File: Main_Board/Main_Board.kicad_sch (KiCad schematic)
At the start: 0 parts

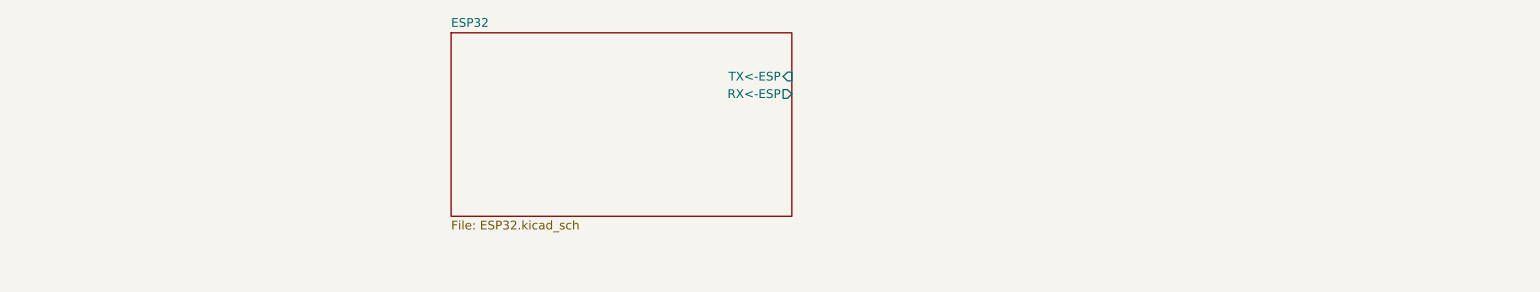
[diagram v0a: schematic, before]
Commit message: PSU Ready + ESP32 advanced
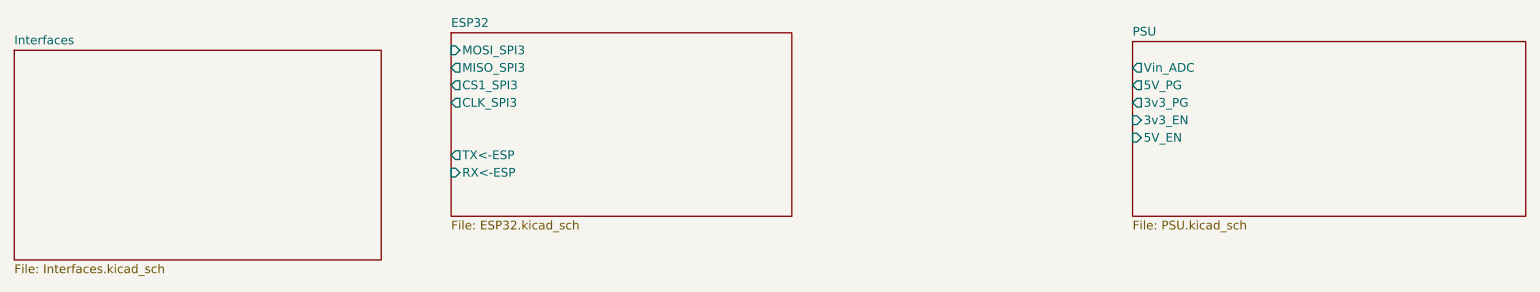
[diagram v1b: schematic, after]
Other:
- added sheet Interfaces (Interfaces.kicad_sch)
- added sheet PSU (PSU.kicad_sch)
- sheet ESP32 ports: added CLK_SPI3, CS1_SPI3, MISO_SPI3, MOSI_SPI3; removed none
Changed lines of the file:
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@@
 	(paper "A4")
+	(sheet
+		(at 190.5 38.1)
+		(size 57.15 25.4)
+		(exclude_from_sim no)
+		(in_bom yes)
+		(on_board yes)
+		(dnp no)
+		(fields_autoplaced yes)
+		(stroke
+			(width 0.1524)
+			(type solid)
+		)
+		(fill
+			(color 0 0 0 0)
+		)
+		(property "Sheetname" "PSU"
+			(at 190.5 37.3884 0)
+			(show_name no)
+			(do_not_autoplace no)
+			(effects
+				(font
+					(size 1.27 1.27)
+				)
+				(justify left bottom)
+			)
+		)
+		(property "Sheetfile" "PSU.kicad_sch"
+			(at 190.5 64.0846 0)
+			(show_name no)
+			(do_not_autoplace no)
+			(effects
+				(font
+					(size 1.27 1.27)
+				)
+				(justify left top)
+			)
+		)
+		(pin "Vin_ADC" output
+			(at 190.5 41.91 180)
+			(effects
+				(font
+					(size 1.27 1.27)
+				)
+				(justify left)
+			)
+		)
+		(pin "5V_PG" output
+			(at 190.5 44.45 180)
+			(effects
+				(font
+					(size 1.27 1.27)
+				)
+				(justify left)
+			)
+		)
+		(pin "3v3_PG" output
+			(at 190.5 46.99 180)
+			(effects
+				(font
+					(size 1.27 1.27)
+				)
+				(justify left)
+			)
+		)
+		(pin "3v3_EN" input
+			(at 190.5 49.53 180)
+			(effects
+				(font
+					(size 1.27 1.27)
+				)
+				(justify left)
+			)
+		)
+		(pin "5V_EN" input
+			(at 190.5 52.07 180)
+			(effects
+				(font
+					(size 1.27 1.27)
+				)
+				(justify left)
+			)
+		)
+		(instances
+			(project "Main_Board"
+				(path "/7481738f-7c20-40bb-99b0-6ccd4168db33"
+					(page "3")
+				)
+			)
+		)
+	)
 	(sheet
 		(at 91.44 36.83)
@@
 			)
 		)
-		(pin "TX<-ESP" input
-			(at 140.97 43.18 0)
-			(effects
-				(font
-					(size 1.27 1.27)
-				)
-				(justify right)
-			)
-		)
-		(pin "RX<-ESP" output
-			(at 140.97 45.72 0)
-			(effects
-				(font
-					(size 1.27 1.27)
-				)
-				(justify right)
+		(pin "TX<-ESP" output
+			(at 91.44 54.61 180)
+			(effects
+				(font
+					(size 1.27 1.27)
+				)
+				(justify left)
+			)
+		)
+		(pin "RX<-ESP" input
+			(at 91.44 57.15 180)
+			(effects
+				(font
+					(size 1.27 1.27)
+				)
+				(justify left)
+			)
+		)
+		(pin "MOSI_SPI3" input
+			(at 91.44 39.37 180)
+			(effects
+				(font
+					(size 1.27 1.27)
+				)
+				(justify left)
+			)
+		)
+		(pin "MISO_SPI3" output
+			(at 91.44 41.91 180)
+			(effects
+				(font
+					(size 1.27 1.27)
+				)
+				(justify left)
+			)
+		)
+		(pin "CS1_SPI3" output
+			(at 91.44 44.45 180)
+			(effects
+				(font
+					(size 1.27 1.27)
+				)
+				(justify left)
+			)
+		)
+		(pin "CLK_SPI3" output
+			(at 91.44 46.99 180)
+			(effects
+				(font
+					(size 1.27 1.27)
+				)
+				(justify left)
 			)
 		)
@@
 				)
 			)
+		)
+	)
+	(sheet
+		(at 27.94 39.37)
+		(size 53.34 30.48)
+		(exclude_from_sim no)
+		(in_bom yes)
+		(on_board yes)
+		(dnp no)
+		(fields_autoplaced yes)
+		(stroke
+			(width 0.1524)
+			(type solid)
+		)
+		(fill
+			(color 0 0 0 0)
+		)
+		(property "Sheetname" "Interfaces"
+			(at 27.94 38.6584 0)
+			(show_name no)
+			(do_not_autoplace no)
+			(effects
+				(font
+					(size 1.27 1.27)
+				)
+				(justify left bottom)
+			)
+		)
+		(property "Sheetfile" "Interfaces.kicad_sch"
+			(at 27.94 70.4346 0)
+			(show_name no)
+			(do_not_autoplace no)
+			(effects
+				(font
+					(size 1.27 1.27)
+				)
+				(justify left top)
+			)
+		)
+		(instances
+			(project "Main_Board"
+				(path "/7481738f-7c20-40bb-99b0-6ccd4168db33"
+					(page "7")
+				)
+			)

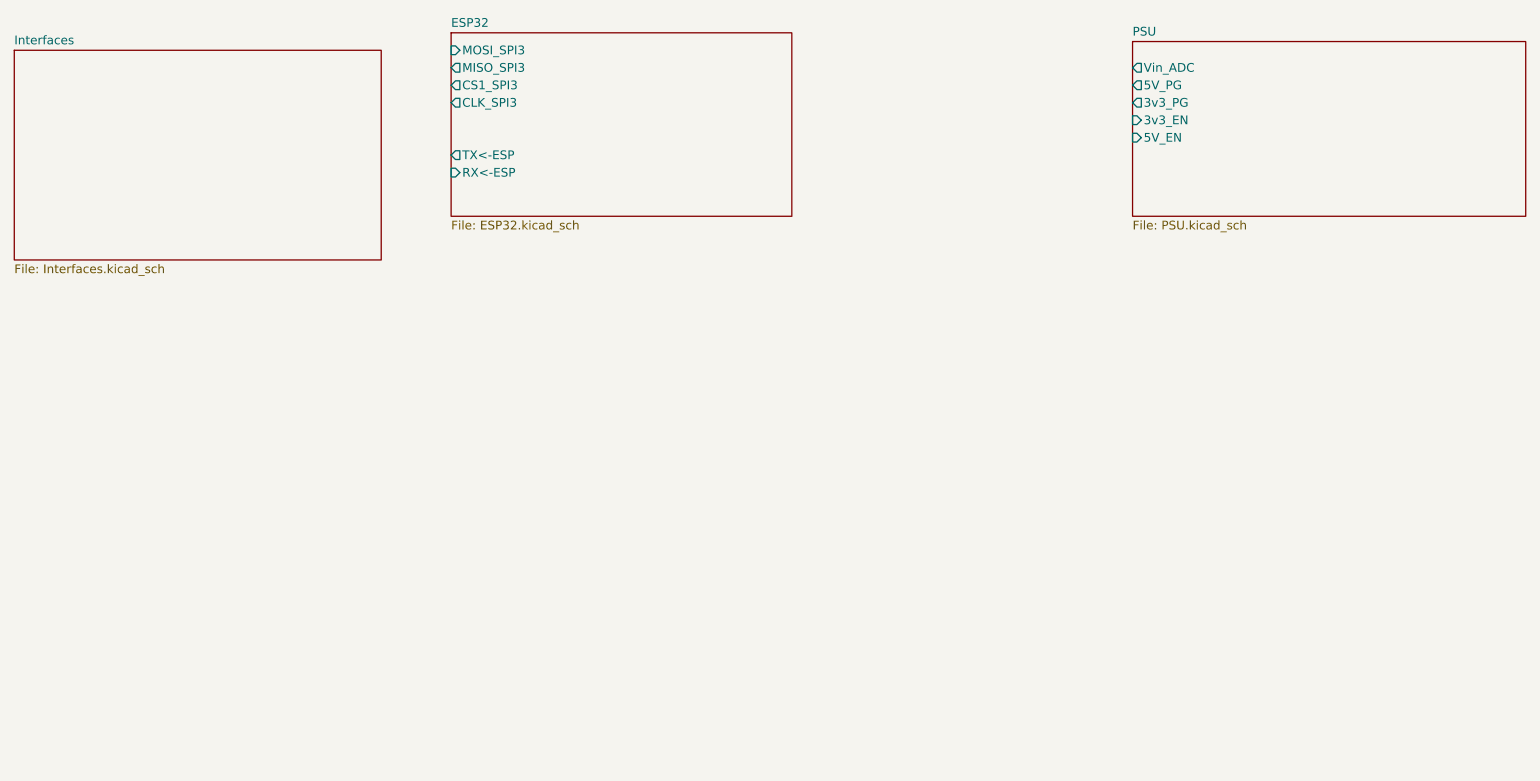
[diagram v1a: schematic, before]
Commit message: Input Protection
Irlm is left to be calculated
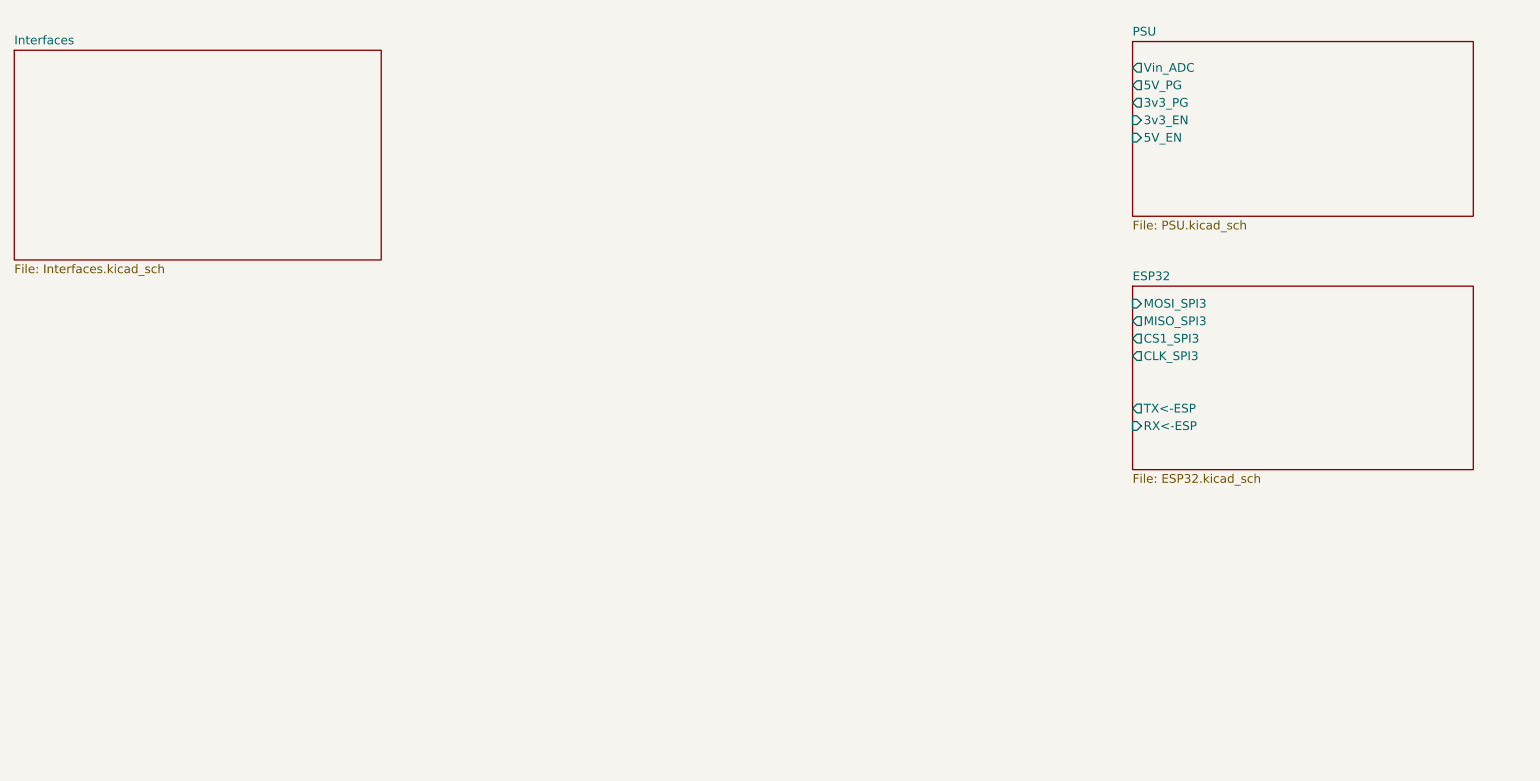
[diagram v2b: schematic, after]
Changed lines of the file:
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@@
 	(sheet
 		(at 190.5 38.1)
-		(size 57.15 25.4)
+		(size 49.53 25.4)
 		(exclude_from_sim no)
 		(in_bom yes)
@@
 	)
 	(sheet
-		(at 91.44 36.83)
+		(at 190.5 73.66)
 		(size 49.53 26.67)
 		(exclude_from_sim no)
@@
 		)
 		(property "Sheetname" "ESP32"
-			(at 91.44 36.1184 0)
+			(at 190.5 72.9484 0)
 			(show_name no)
 			(do_not_autoplace no)
@@
 		)
 		(property "Sheetfile" "ESP32.kicad_sch"
-			(at 91.44 64.0846 0)
+			(at 190.5 100.9146 0)
 			(show_name no)
 			(do_not_autoplace no)
@@
 		)
 		(pin "TX<-ESP" output
-			(at 91.44 54.61 180)
+			(at 190.5 91.44 180)
 			(effects
 				(font
@@
 		)
 		(pin "RX<-ESP" input
-			(at 91.44 57.15 180)
+			(at 190.5 93.98 180)
 			(effects
 				(font
@@
 		)
 		(pin "MOSI_SPI3" input
-			(at 91.44 39.37 180)
+			(at 190.5 76.2 180)
 			(effects
 				(font
@@
 		)
 		(pin "MISO_SPI3" output
-			(at 91.44 41.91 180)
+			(at 190.5 78.74 180)
 			(effects
 				(font
@@
 		)
 		(pin "CS1_SPI3" output
-			(at 91.44 44.45 180)
+			(at 190.5 81.28 180)
 			(effects
 				(font
@@
 		)
 		(pin "CLK_SPI3" output
-			(at 91.44 46.99 180)
+			(at 190.5 83.82 180)
 			(effects
 				(font

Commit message: RS485 Transciever + Input Protection fix
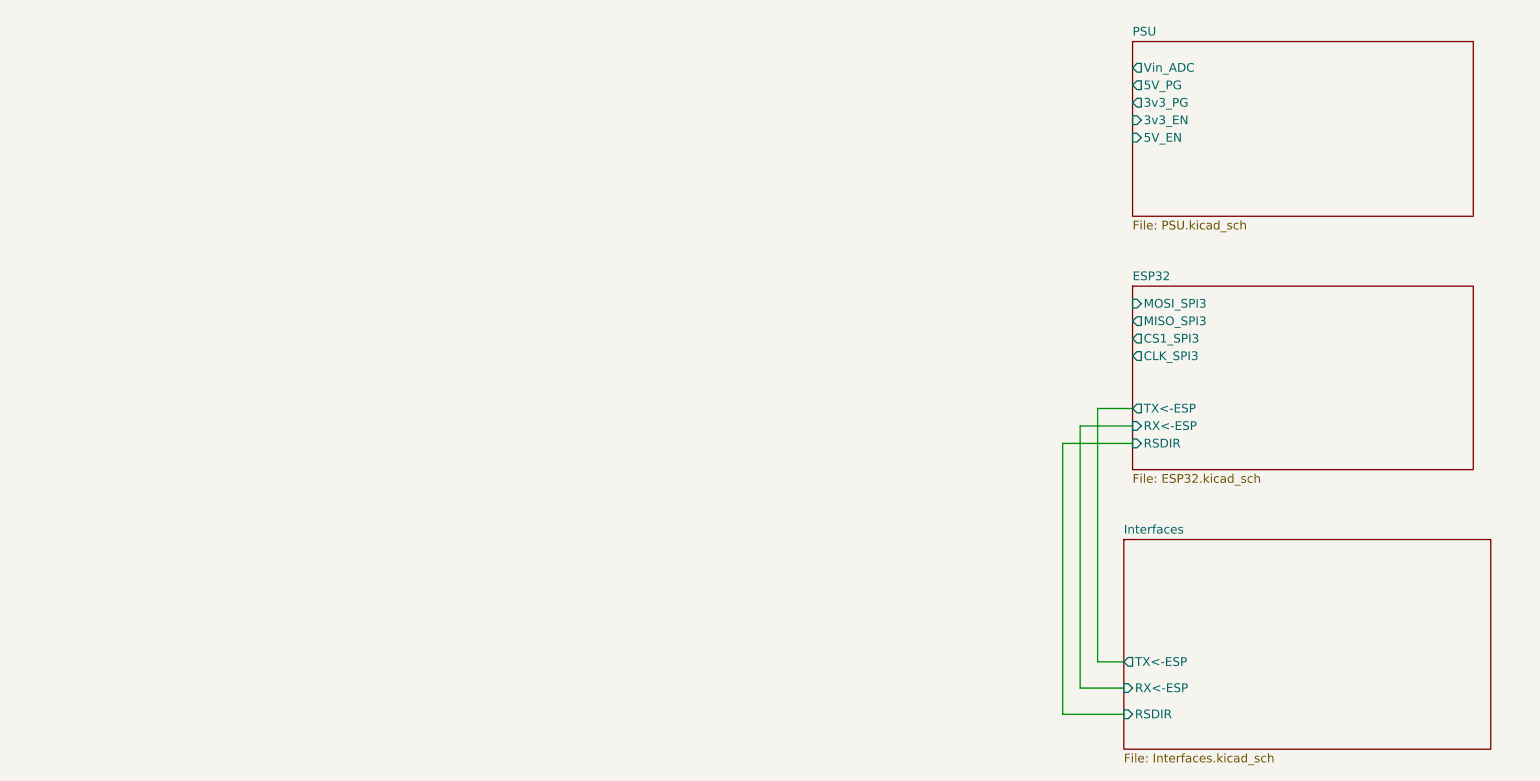
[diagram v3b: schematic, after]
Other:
- sheet ESP32 ports: added RSDIR; removed none
- sheet Interfaces ports: added RSDIR, RX<-ESP, TX<-ESP; removed none
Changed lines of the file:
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@@
 	(generator_version "10.0")
 	(paper "A4")
+	(wire
+		(pts
+			(xy 190.5 93.98) (xy 182.88 93.98)
+		)
+		(stroke
+			(width 0)
+			(type default)
+		)
+	)
+	(wire
+		(pts
+			(xy 180.34 96.52) (xy 180.34 135.89)
+		)
+		(stroke
+			(width 0)
+			(type default)
+		)
+	)
+	(wire
+		(pts
+			(xy 185.42 91.44) (xy 185.42 128.27)
+		)
+		(stroke
+			(width 0)
+			(type default)
+		)
+	)
+	(wire
+		(pts
+			(xy 190.5 91.44) (xy 185.42 91.44)
+		)
+		(stroke
+			(width 0)
+			(type default)
+		)
+	)
+	(wire
+		(pts
+			(xy 190.5 96.52) (xy 180.34 96.52)
+		)
+		(stroke
+			(width 0)
+			(type default)
+		)
+	)
+	(wire
+		(pts
+			(xy 182.88 93.98) (xy 182.88 132.08)
+		)
+		(stroke
+			(width 0)
+			(type default)
+		)
+	)
+	(wire
+		(pts
+			(xy 182.88 132.08) (xy 189.23 132.08)
+		)
+		(stroke
+			(width 0)
+			(type default)
+		)
+	)
+	(wire
+		(pts
+			(xy 180.34 135.89) (xy 189.23 135.89)
+		)
+		(stroke
+			(width 0)
+			(type default)
+		)
+	)
+	(wire
+		(pts
+			(xy 185.42 128.27) (xy 189.23 128.27)
+		)
+		(stroke
+			(width 0)
+			(type default)
+		)
+	)
 	(sheet
 		(at 190.5 38.1)
@@
 			)
 		)
+		(pin "RSDIR" input
+			(at 190.5 96.52 180)
+			(effects
+				(font
+					(size 1.27 1.27)
+				)
+				(justify left)
+			)
+		)
 		(instances
 			(project "Main_Board"
@@
 	)
 	(sheet
-		(at 27.94 39.37)
+		(at 189.23 110.49)
 		(size 53.34 30.48)
 		(exclude_from_sim no)
@@
 		)
 		(property "Sheetname" "Interfaces"
-			(at 27.94 38.6584 0)
+			(at 189.23 109.7784 0)
 			(show_name no)
 			(do_not_autoplace no)
@@
 		)
 		(property "Sheetfile" "Interfaces.kicad_sch"
-			(at 27.94 70.4346 0)
+			(at 189.23 141.5546 0)
 			(show_name no)
 			(do_not_autoplace no)
@@
 			)
 		)
+		(pin "RSDIR" input
+			(at 189.23 135.89 180)
+			(effects
+				(font
+					(size 1.27 1.27)
+				)
+				(justify left)
+			)
+		)
+		(pin "RX<-ESP" input
+			(at 189.23 132.08 180)
+			(effects
+				(font
+					(size 1.27 1.27)
+				)
+				(justify left)
+			)
+		)
+		(pin "TX<-ESP" output
+			(at 189.23 128.27 180)
+			(effects
+				(font
+					(size 1.27 1.27)
+				)
+				(justify left)
+			)
+		)

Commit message: Aesthetics/cleanup
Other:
- sheet ESP32 ports: added MODULE_BUS_DIR, MODULE_BUS_RX, MODULE_BUS_TX; removed RSDIR, RX<-ESP, TX<-ESP
- sheet Interfaces ports: added MODULE_BUS_DIR, MODULE_BUS_RX, MODULE_BUS_TX; removed RSDIR, RX<-ESP, TX<-ESP
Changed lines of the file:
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@@
 	(generator_version "10.0")
 	(paper "A4")
-	(wire
-		(pts
-			(xy 190.5 93.98) (xy 182.88 93.98)
-		)
-		(stroke
-			(width 0)
-			(type default)
-		)
-	)
-	(wire
-		(pts
-			(xy 180.34 96.52) (xy 180.34 135.89)
-		)
-		(stroke
-			(width 0)
-			(type default)
-		)
-	)
-	(wire
-		(pts
-			(xy 185.42 91.44) (xy 185.42 128.27)
-		)
-		(stroke
-			(width 0)
-			(type default)
-		)
-	)
-	(wire
-		(pts
-			(xy 190.5 91.44) (xy 185.42 91.44)
-		)
-		(stroke
-			(width 0)
-			(type default)
-		)
-	)
-	(wire
-		(pts
-			(xy 190.5 96.52) (xy 180.34 96.52)
-		)
-		(stroke
-			(width 0)
-			(type default)
-		)
-	)
-	(wire
-		(pts
-			(xy 182.88 93.98) (xy 182.88 132.08)
-		)
-		(stroke
-			(width 0)
-			(type default)
-		)
-	)
-	(wire
-		(pts
-			(xy 182.88 132.08) (xy 189.23 132.08)
-		)
-		(stroke
-			(width 0)
-			(type default)
-		)
-	)
-	(wire
-		(pts
-			(xy 180.34 135.89) (xy 189.23 135.89)
-		)
-		(stroke
-			(width 0)
-			(type default)
-		)
-	)
-	(wire
-		(pts
-			(xy 185.42 128.27) (xy 189.23 128.27)
-		)
-		(stroke
-			(width 0)
-			(type default)
+	(bus_entry
+		(at 182.88 91.44)
+		(size -2.54 2.54)
+		(stroke
+			(width 0)
+			(type default)
+		)
+	)
+	(bus_entry
+		(at 182.88 130.81)
+		(size -2.54 2.54)
+		(stroke
+			(width 0)
+			(type default)
+		)
+	)
+	(bus_entry
+		(at 182.88 96.52)
+		(size -2.54 2.54)
+		(stroke
+			(width 0)
+			(type default)
+		)
+	)
+	(bus_entry
+		(at 182.88 93.98)
+		(size -2.54 2.54)
+		(stroke
+			(width 0)
+			(type default)
+		)
+	)
+	(bus_entry
+		(at 182.88 133.35)
+		(size -2.54 2.54)
+		(stroke
+			(width 0)
+			(type default)
+		)
+	)
+	(bus_entry
+		(at 182.88 135.89)
+		(size -2.54 2.54)
+		(stroke
+			(width 0)
+			(type default)
+		)
+	)
+	(wire
+		(pts
+			(xy 182.88 91.44) (xy 189.23 91.44)
+		)
+		(stroke
+			(width 0)
+			(type default)
+		)
+	)
+	(wire
+		(pts
+			(xy 182.88 133.35) (xy 189.23 133.35)
+		)
+		(stroke
+			(width 0)
+			(type default)
+		)
+	)
+	(wire
+		(pts
+			(xy 182.88 130.81) (xy 189.23 130.81)
+		)
+		(stroke
+			(width 0)
+			(type default)
+		)
+	)
+	(bus
+		(pts
+			(xy 180.34 93.98) (xy 180.34 99.06)
+		)
+		(stroke
+			(width 0)
+			(type default)
+		)
+	)
+	(wire
+		(pts
+			(xy 182.88 135.89) (xy 189.23 135.89)
+		)
+		(stroke
+			(width 0)
+			(type default)
+		)
+	)
+	(wire
+		(pts
+			(xy 182.88 96.52) (xy 189.23 96.52)
+		)
+		(stroke
+			(width 0)
+			(type default)
+		)
+	)
+	(wire
+		(pts
+			(xy 182.88 93.98) (xy 189.23 93.98)
+		)
+		(stroke
+			(width 0)
+			(type default)
+		)
+	)
+	(bus
+		(pts
+			(xy 180.34 135.89) (xy 180.34 138.43)
+		)
+		(stroke
+			(width 0)
+			(type default)
+		)
+	)
+	(bus
+		(pts
+			(xy 180.34 99.06) (xy 180.34 135.89)
+		)
+		(stroke
+			(width 0)
+			(type default)
+		)
+	)
+	(label "MODBUS_DIR"
+		(at 182.88 96.52 0)
+		(effects
+			(font
+				(size 0.508 0.508)
+			)
+			(justify left bottom)
+		)
+	)
+	(label "MODBUS_RX"
+		(at 182.88 91.44 0)
+		(effects
+			(font
+				(size 0.508 0.508)
+			)
+			(justify left bottom)
+		)
+	)
+	(label "MODBUS_DIR"
+		(at 182.88 135.89 0)
+		(effects
+			(font
+				(size 0.508 0.508)
+			)
+			(justify left bottom)
+		)
+	)
+	(label "MODBUS_TX"
+		(at 182.88 133.35 0)
+		(effects
+			(font
+				(size 0.508 0.508)
+			)
+			(justify left bottom)
+		)
+	)
+	(label "MODBUS_TX"
+		(at 182.88 93.98 0)
+		(effects
+			(font
+				(size 0.508 0.508)
+			)
+			(justify left bottom)
+		)
+	)
+	(label "MODBUS_RX"
+		(at 182.88 130.81 0)
+		(effects
+			(font
+				(size 0.508 0.508)
+			)
+			(justify left bottom)
 		)
 	)
@@
 	)
 	(sheet
-		(at 190.5 73.66)
+		(at 189.23 73.66)
 		(size 49.53 26.67)
 		(exclude_from_sim no)
@@
 		)
 		(property "Sheetname" "ESP32"
-			(at 190.5 72.9484 0)
+			(at 189.23 72.9484 0)
 			(show_name no)
 			(do_not_autoplace no)
@@
 		)
 		(property "Sheetfile" "ESP32.kicad_sch"
-			(at 190.5 100.9146 0)
+			(at 189.23 100.9146 0)
 			(show_name no)
 			(do_not_autoplace no)
@@
 			)
 		)
-		(pin "TX<-ESP" output
-			(at 190.5 91.44 180)
-			(effects
-				(font
-					(size 1.27 1.27)
-				)
-				(justify left)
-			)
-		)
-		(pin "RX<-ESP" input
-			(at 190.5 93.98 180)
-			(effects
-				(font
-					(size 1.27 1.27)
-				)
-				(justify left)
-			)
-		)
 		(pin "MOSI_SPI3" input
-			(at 190.5 76.2 180)
+			(at 189.23 76.2 180)
 			(effects
 				(font
@@
 		)
 		(pin "MISO_SPI3" output
-			(at 190.5 78.74 180)
+			(at 189.23 78.74 180)
 			(effects
 				(font
@@
 		)
 		(pin "CS1_SPI3" output
-			(at 190.5 81.28 180)
+			(at 189.23 81.28 180)
 			(effects
 				(font
@@
 		)
 		(pin "CLK_SPI3" output
-			(at 190.5 83.82 180)
-			(effects
-				(font
-					(size 1.27 1.27)
-				)
-				(justify left)
-			)
-		)
-		(pin "RSDIR" input
-			(at 190.5 96.52 180)
+			(at 189.23 83.82 180)
+			(effects
+				(font
+					(size 1.27 1.27)
+				)
+				(justify left)
+			)
+		)
+		(pin "MODULE_BUS_RX" input
+			(at 189.23 91.44 180)
+			(effects
+				(font
+					(size 1.27 1.27)
+				)
+				(justify left)
+			)
+		)
+		(pin "MODULE_BUS_DIR" input
+			(at 189.23 96.52 180)
+			(effects
+				(font
+					(size 1.27 1.27)
+				)
+				(justify left)
+			)
+		)
+		(pin "MODULE_BUS_TX" output
+			(at 189.23 93.98 180)
 			(effects
 				(font
@@
 			)
 		)
-		(pin "RSDIR" input
+		(pin "MODULE_BUS_RX" input
+			(at 189.23 130.81 180)
+			(effects
+				(font
+					(size 1.27 1.27)
+				)
+				(justify left)
+			)
+		)
+		(pin "MODULE_BUS_TX" output
+			(at 189.23 133.35 180)
+			(effects
+				(font
+					(size 1.27 1.27)
+				)
+				(justify left)
+			)
+		)
+		(pin "MODULE_BUS_DIR" input
 			(at 189.23 135.89 180)
 			(effects
 				(font
-					(size 1.27 1.27)
-				)
-				(justify left)
-			)
-		)
-		(pin "RX<-ESP" input
-			(at 189.23 132.08 180)
-			(effects
-				(font
-					(size 1.27 1.27)
-				)
-				(justify left)
-			)
-		)
-		(pin "TX<-ESP" output
-			(at 189.23 128.27 180)
-			(effects
-				(font
